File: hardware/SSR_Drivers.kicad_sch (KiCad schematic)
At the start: 22 parts

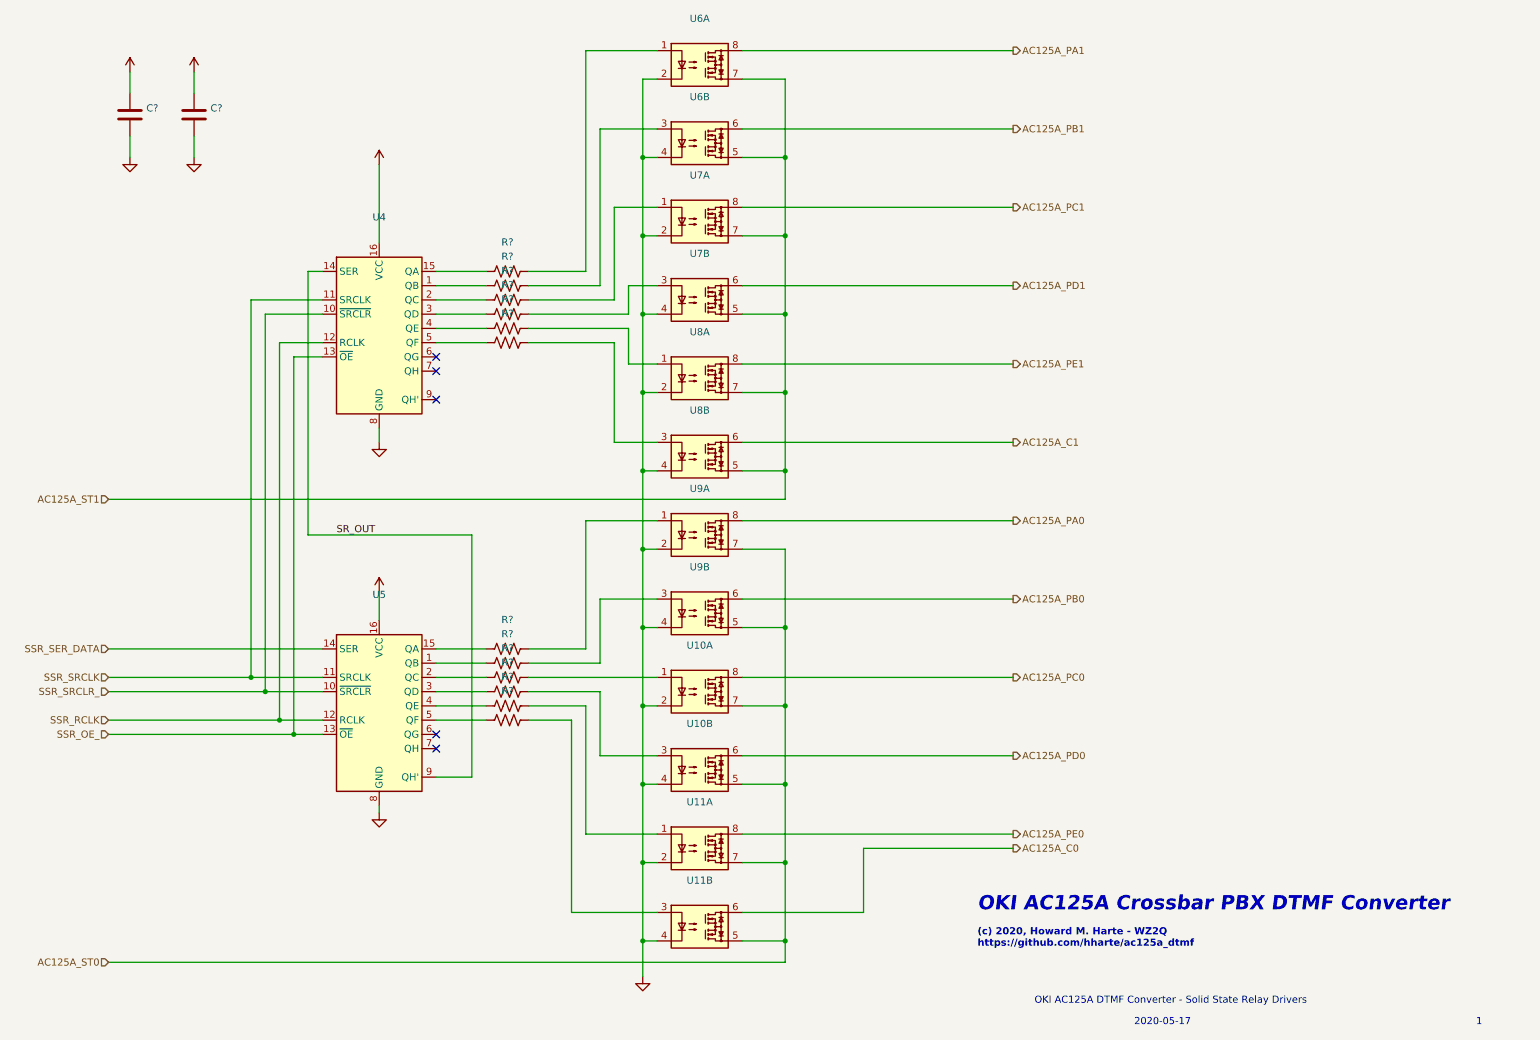
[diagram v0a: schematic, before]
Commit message: Fix a couple DRC errors in the layout.
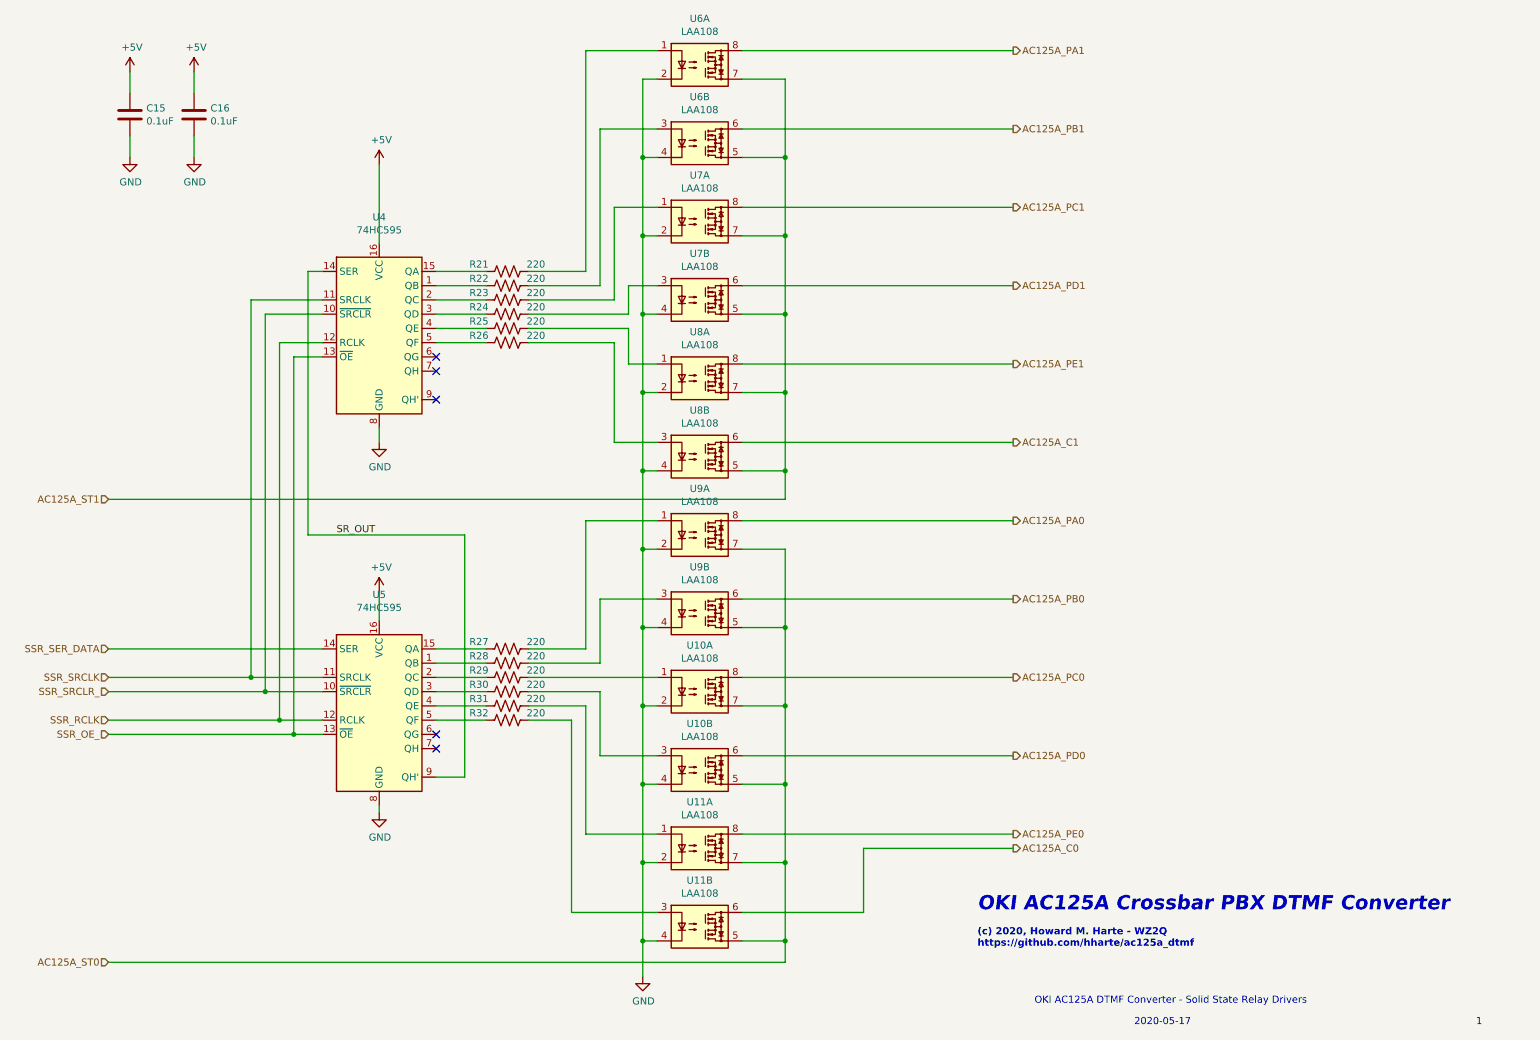
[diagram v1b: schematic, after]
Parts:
- C15, C16: renamed from C?; value (none) -> 0.1uF; footprint (none) -> Capacitor_THT:C_Disc_D3.0mm_W2.0mm_P2.50mm
- R21, R22, R23, R24, R25, R26, R27, R28, R29, R30, R31, R32: renamed from R?; value (none) -> 220; footprint (none) -> Resistor_THT:R_Axial_DIN0207_L6.3mm_D2.5mm_P7.62mm_Horizontal
- U10, U11, U6, U7, U8, U9: value (none) -> LAA108; footprint (none) -> Package_DIP:DIP-8_W7.62mm
- U4, U5: value (none) -> 74HC595; footprint (none) -> Package_DIP:DIP-16_W7.62mm
